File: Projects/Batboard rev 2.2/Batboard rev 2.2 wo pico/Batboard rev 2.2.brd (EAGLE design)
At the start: 101.6 x 68.6 mm, 61 parts, among them J1 1X2-3.5MM, J2 1X2-3.5MM, J3 1X2-3.5MM, J4 1X2-3.5MM, J5 1X2-3.5MM, J6 1X2-3.5MM, U2 TL3472CD, X1 22-23-2081, X17 22-23-2081

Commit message: Updated
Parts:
- moved TPS1 143.0 mm to (31.3, 6.99)
- moved C4 115.4 mm to (30.6, 11.1), turned to 180 degrees
- moved R25 106.0 mm to (2.22, 44.5), turned to 270 degrees
- moved C5 105.1 mm to (25.2, 8.41), turned to 180 degrees
- moved SRR1260-100M1 100.7 mm to (47.1, 7.14), turned to 270 degrees
- moved R5 99.9 mm to (27.3, 2.86)
- moved R3 98.5 mm to (32.4, 2.86)
- moved R6 98.2 mm to (25.2, 5.56), turned to 180 degrees
- moved SHOTTKY1 98.2 mm to (36.5, 11.3)
- moved R7 85.0 mm to (36.4, 7.30), turned to 90 degrees
- moved C9 81.9 mm to (37.5, 2.86)
- moved C6 80.6 mm to (39.2, 7.30), turned to 270 degrees
- moved U$7 74.6 mm to (66.8, 9.21)
- moved R12 73.1 mm to (59.2, 4.60), turned to 90 degrees
- moved C21 72.2 mm to (68.9, 3.49), turned to 270 degrees
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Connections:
- removed net 12V: C2.2, U$5.14
- net +12V: now also C2.2, U$5.14
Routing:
- net +12V: track 104.7 -> 226.7 mm, vias 3 -> 4
- net +5V: track 61.0 -> 103.1 mm, vias 0 -> 1
- net -12V: track 12.1 -> 49.1 mm, vias 1 -> 2
- net N$14: track 19.8 -> 43.5 mm
- net N$16: track 19.3 -> 40.4 mm
- net N$53: track 0.00 -> 20.7 mm
- net N$58: track 0.00 -> 19.7 mm
- net N$18: track 17.6 -> 37.2 mm
- net N$19: track 16.5 -> 34.1 mm
- net N$23: track 15.9 -> 30.9 mm
- net N$27: track 15.4 -> 29.7 mm
- net BATT: track 0.00 -> 13.2 mm
- net N$28: track 15.3 -> 25.8 mm, vias 0 -> 1
- net N$13: track 18.0 -> 26.2 mm
- net N$54: track 0.00 -> 7.82 mm
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
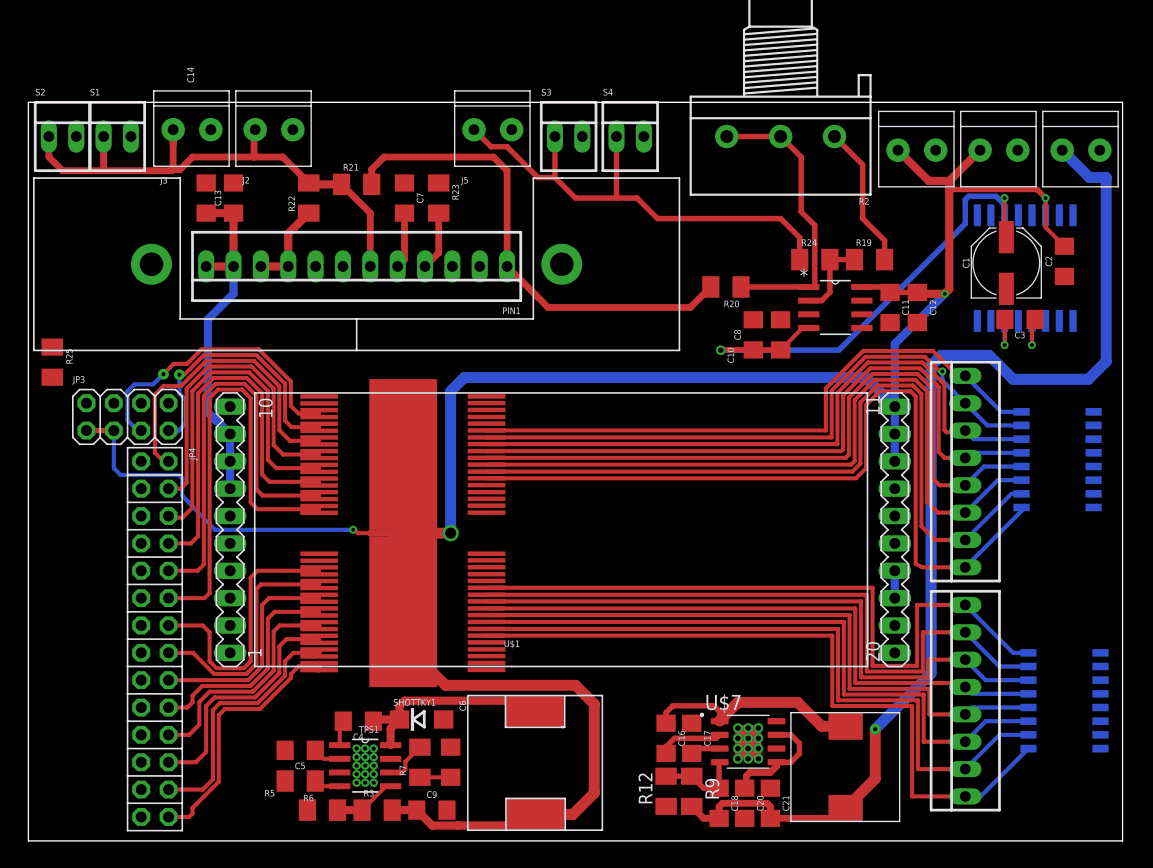
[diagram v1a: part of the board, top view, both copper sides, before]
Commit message: Checked ERC and DRC
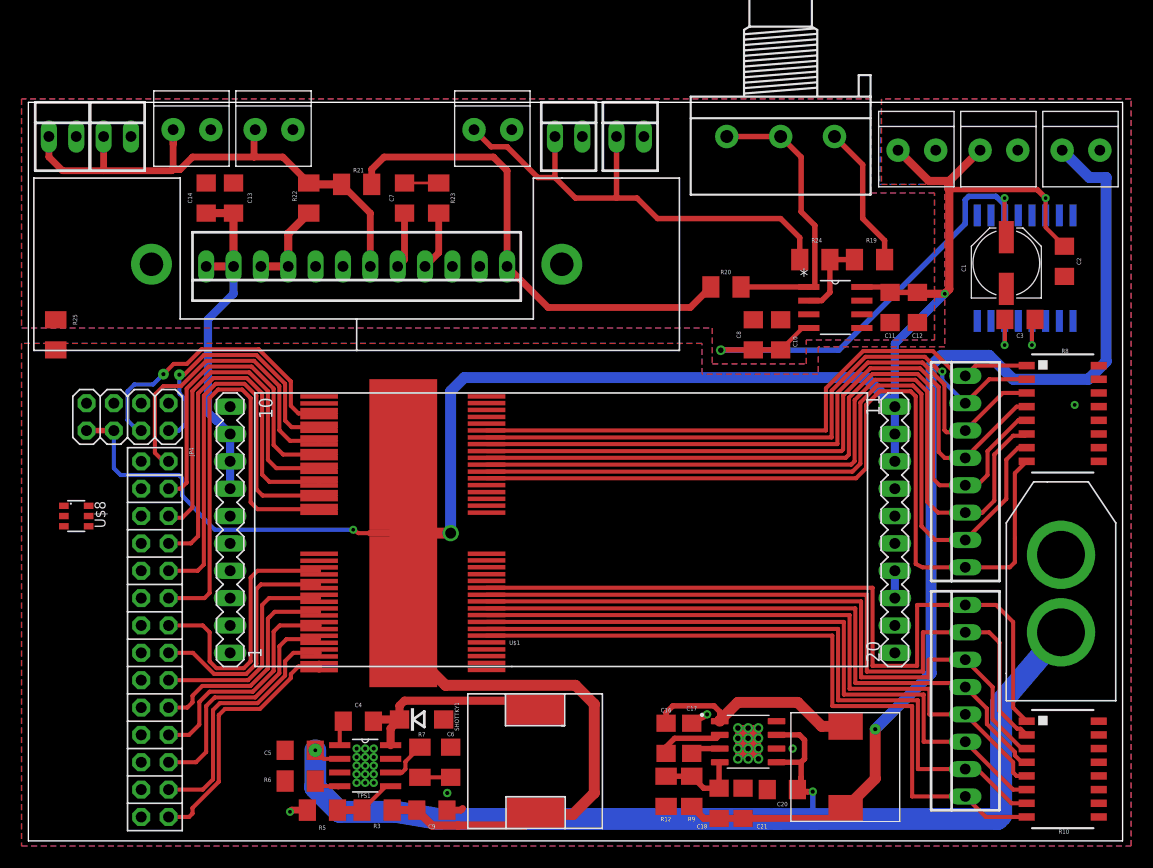
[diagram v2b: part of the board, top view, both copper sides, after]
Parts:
- added U$6: XT60, ultravolt_daughterboard:XT60
- added U$8: DMN2004DMK_DUAL_N-CHANNEL_MOSFET_ARRAY, ultravolt_daughterboard:SOT23-6
- R10, R8: value (none) -> 10K
- moved R10 6.35 mm to (96.0, 6.67), flipped to the top, turned to 270 degrees
- moved R8 4.31 mm to (96.0, 39.7), flipped to the top, turned to 270 degrees
- moved C20 3.72 mm to (70.0, 4.76), turned to 180 degrees
- moved R25 2.56 mm to (2.54, 47.0)
- moved C21 2.54 mm to (66.4, 3.49)
- moved SRR1260-100M1 0.16 mm to (47.1, 7.30)
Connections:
- removed net N$31: U$5.5
- net BATT: now also U$6.POS
- net GND: now also U$5.5, U$6.NEG
- net N$2: now also R10.8; no longer R10.1
- net N$3: now also R10.7; no longer R10.2
- net N$30: now also R8.8; no longer R8.1
- net N$32: now also R10.1; no longer R10.8
- net N$33: now also R10.2; no longer R10.7
- net N$35: now also R10.6; no longer R10.3
- net N$36: now also R10.3; no longer R10.6
- net N$37: now also R10.4; no longer R10.5
- net N$38: now also R10.5; no longer R10.4
- net N$39: now also R8.1; no longer R8.8
- net N$40: now also R8.2; no longer R8.7
- net N$41: now also R8.7; no longer R8.2
- net N$42: now also R8.6; no longer R8.3
- net N$43: now also R8.3; no longer R8.6
- net N$44: now also R8.4; no longer R8.5
- net N$45: now also R8.5; no longer R8.4
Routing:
- net BATT: track 13.2 -> 106.6 mm, vias 0 -> 2
- net N$32: track 65.1 -> 72.2 mm
- net N$30: track 74.8 -> 81.7 mm
- net N$33: track 62.4 -> 68.6 mm
- net GND: track 0.00 -> 4.86 mm, vias 0 -> 5
- net N$42: track 68.6 -> 73.4 mm
- net N$41: track 71.2 -> 75.6 mm
- net N$36: track 60.2 -> 64.5 mm
- net N$37: track 57.9 -> 61.7 mm
- net N$45: track 65.9 -> 69.4 mm
- net N$26: track 0.00 -> 3.18 mm
- net N$38: track 60.4 -> 62.9 mm
- net +5V: track 103.1 -> 100.7 mm
- net N$44: track 63.0 -> 65.2 mm
- net N$35: track 62.2 -> 64.1 mm
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- added copper zone on layer 1, net GND
- added copper zone on layer 16, net GND

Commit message: BOM generation started
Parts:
- added SV1: (no value), con-lstb:MA03-1
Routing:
- net N$9: track 21.4 -> 23.0 mm
- net N$8: track 22.2 -> 23.8 mm
- net N$7: track 23.3 -> 24.9 mm
- net N$6: track 24.5 -> 26.0 mm
- net N$5: track 24.5 -> 26.1 mm
- net N$13: track 26.2 -> 27.7 mm
- net N$12: track 23.0 -> 24.5 mm
- net N$11: track 21.1 -> 22.7 mm
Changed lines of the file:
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@@
 <drawing>
 <settings>
-<setting alwaysvectorfont="yes"/>
+<setting alwaysvectorfont="no"/>
 <setting verticaltext="up"/>
 </settings>
@@
 <attribute name="NAME" x="6.147" y="31.5595" size="1.016" layer="25" ratio="10" rot="R270"/>
 </element>
+<element name="SV1" library="con-lstb" library_urn="urn:adsk.eagle:library:162" package="MA03-1" package3d_urn="urn:adsk.eagle:package:8339/1" value="" x="5.08" y="21.2725" rot="R90">
+<attribute name="MF" value="" x="5.08" y="21.2725" size="1.778" layer="27" rot="R90" display="off"/>
+<attribute name="MPN" value="" x="5.08" y="21.2725" size="1.778" layer="27" rot="R90" display="off"/>
+<attribute name="OC_FARNELL" value="unknown" x="5.08" y="21.2725" size="1.778" layer="27" rot="R90" display="off"/>
+<attribute name="OC_NEWARK" value="unknown" x="5.08" y="21.2725" size="1.778" layer="27" rot="R90" display="off"/>
+</element>
 </elements>
 <signals>
@@
 <wire x1="83.6075" y1="61.2775" x2="85.5125" y2="61.2775" width="0.762" layer="1"/>
 <wire x1="85.5125" y1="61.2775" x2="85.5125" y2="60.48375" width="0.762" layer="1"/>
-<wire x1="85.5125" y1="60.48375" x2="85.5125" y2="51.2225" width="0.762" layer="1"/>
+<wire x1="85.5125" y1="51.2225" x2="85.5125" y2="60.48375" width="0.762" layer="1"/>
 <wire x1="85.5125" y1="51.2225" x2="85.09" y2="50.8" width="0.762" layer="1"/>
 <wire x1="14.2875" y1="32.0675" x2="17.30375" y2="28.8925" width="0.381" layer="16"/>
@@
 <contactref element="U$2" pad="P$36"/>
 <contactref element="U$2" pad="P$35"/>
-<wire x1="26.994" y1="16.493" x2="26.994" y2="16.1925" width="0.508" layer="1"/>
-<wire x1="26.994" y1="16.1925" x2="26.994" y2="15.859" width="0.508" layer="1"/>
 <wire x1="13.024" y1="2.2225" x2="13.0175" y2="2.2225" width="0.508" layer="1"/>
 <wire x1="25.0825" y1="16.1925" x2="26.994" y2="16.1925" width="0.381" layer="1"/>
@@
 <wire x1="13.0175" y1="2.2225" x2="14.9225" y2="2.2225" width="0.381" layer="1"/>
 <wire x1="14.9225" y1="2.2225" x2="15.24" y2="2.54" width="0.381" layer="1"/>
+<wire x1="26.994" y1="16.1925" x2="28.575" y2="16.1925" width="0.381" layer="1"/>
+<wire x1="26.994" y1="16.1925" x2="26.994" y2="16.493" width="0.254" layer="1"/>
+<wire x1="26.994" y1="16.1925" x2="26.994" y2="15.859" width="0.254" layer="1"/>
 </signal>
 <signal name="N$6">
@@
 <wire x1="17.145" y1="5.715" x2="16.1925" y2="4.7625" width="0.381" layer="1"/>
 <wire x1="16.1925" y1="4.7625" x2="13.0175" y2="4.7625" width="0.381" layer="1"/>
+<wire x1="26.994" y1="17.4625" x2="28.575" y2="17.4625" width="0.381" layer="1"/>
 </signal>
 <signal name="N$7">
@@
 <wire x1="16.51" y1="8.255" x2="15.5575" y2="7.3025" width="0.381" layer="1"/>
 <wire x1="15.5575" y1="7.3025" x2="13.0175" y2="7.3025" width="0.381" layer="1"/>
+<wire x1="26.994" y1="18.7325" x2="28.575" y2="18.7325" width="0.381" layer="1"/>
 </signal>
 <signal name="N$8">
@@
 <wire x1="15.875" y1="10.795" x2="14.9225" y2="9.8425" width="0.381" layer="1"/>
 <wire x1="14.9225" y1="9.8425" x2="13.0175" y2="9.8425" width="0.381" layer="1"/>
+<wire x1="26.994" y1="20.0025" x2="28.575" y2="20.0025" width="0.381" layer="1"/>
 </signal>
 <signal name="N$9">
@@
 <wire x1="22.8727" y1="21.2725" x2="22.3901" y2="20.7899" width="0.381" layer="1"/>
 <wire x1="22.3901" y1="20.7899" x2="22.2377" y2="20.6375" width="0.381" layer="1"/>
+<wire x1="26.994" y1="21.2725" x2="28.575" y2="21.2725" width="0.381" layer="1"/>
 </signal>
 <signal name="N$11">
@@
 <wire x1="22.3393" y1="22.5425" x2="21.7043" y2="21.9075" width="0.381" layer="1"/>
 <wire x1="26.994" y1="22.5425" x2="22.3393" y2="22.5425" width="0.381" layer="1"/>
+<wire x1="26.994" y1="22.5425" x2="28.575" y2="22.5425" width="0.381" layer="1"/>
 </signal>
 <signal name="N$12">
@@
 <wire x1="17.24155625" y1="15.50035" x2="15.27940625" y2="17.4625" width="0.381" layer="1"/>
 <wire x1="15.27940625" y1="17.4625" x2="13.0175" y2="17.4625" width="0.381" layer="1"/>
+<wire x1="26.994" y1="23.8125" x2="28.575" y2="23.8125" width="0.381" layer="1"/>
 </signal>
 <signal name="N$13">
@@
 <wire x1="26.994" y1="24.745" x2="26.994" y2="25.0825" width="0.254" layer="1"/>
 <wire x1="26.994" y1="25.0825" x2="26.994" y2="25.395" width="0.254" layer="1"/>
-<wire x1="26.994" y1="25.0825" x2="21.2725" y2="25.0825" width="0.381" layer="1"/>
+<wire x1="26.994" y1="25.0825" x2="26.82875" y2="25.0825" width="0.381" layer="1"/>
+<wire x1="26.82875" y1="25.0825" x2="21.2725" y2="25.0825" width="0.381" layer="1"/>
 <wire x1="21.2725" y1="25.0825" x2="20.6375" y2="24.4475" width="0.381" layer="1"/>
 <wire x1="20.6375" y1="24.4475" x2="20.6375" y2="16.66875" width="0.381" layer="1"/>
@@
 <wire x1="16.8275" y1="19.3675" x2="16.1925" y2="20.0025" width="0.381" layer="1"/>
 <wire x1="16.1925" y1="20.0025" x2="13.0175" y2="20.0025" width="0.381" layer="1"/>
+<wire x1="26.994" y1="25.0825" x2="28.575" y2="25.0825" width="0.381" layer="1"/>
 </signal>
 <signal name="N$14">

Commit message: Updated BOM
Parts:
- moved C9 4.13 mm to (33.3, 2.86)
- moved SHOTTKY1 4.13 mm to (32.4, 11.3)
- moved C4 4.13 mm to (26.5, 11.1)
- moved C5 4.13 mm to (21.1, 8.41)
- moved R5 4.13 mm to (23.2, 2.86)
- moved R6 4.13 mm to (21.1, 5.56)
- moved TPS1 4.13 mm to (27.1, 6.99)
- moved C6 4.13 mm to (35.1, 7.30)
- moved R3 4.13 mm to (28.3, 2.86)
- moved R7 4.13 mm to (32.2, 7.30)
- moved SRR1260-100M1 4.13 mm to (43.0, 7.30)
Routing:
- net BATT: track 106.6 -> 76.2 mm
- net +12V: track 226.8 -> 215.2 mm

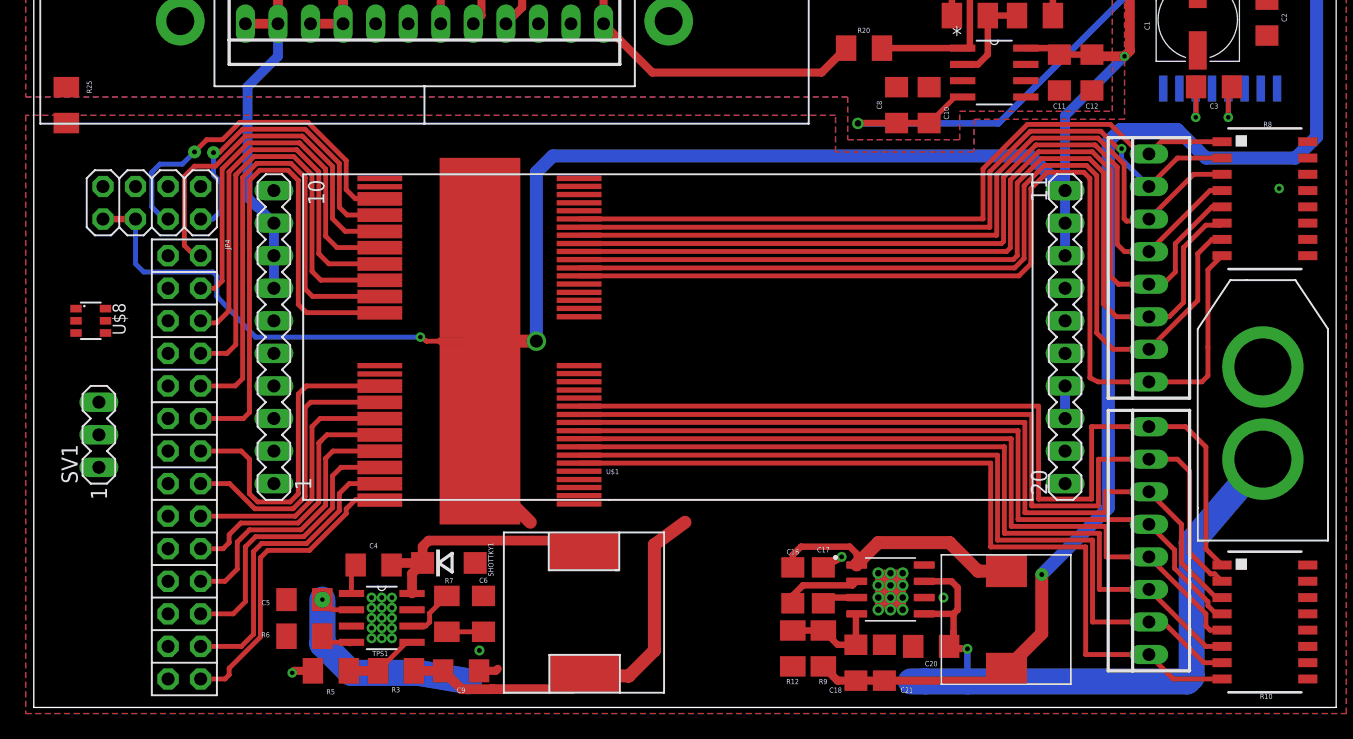
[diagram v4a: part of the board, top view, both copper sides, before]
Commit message: Updated capacitors for switching step down regulators
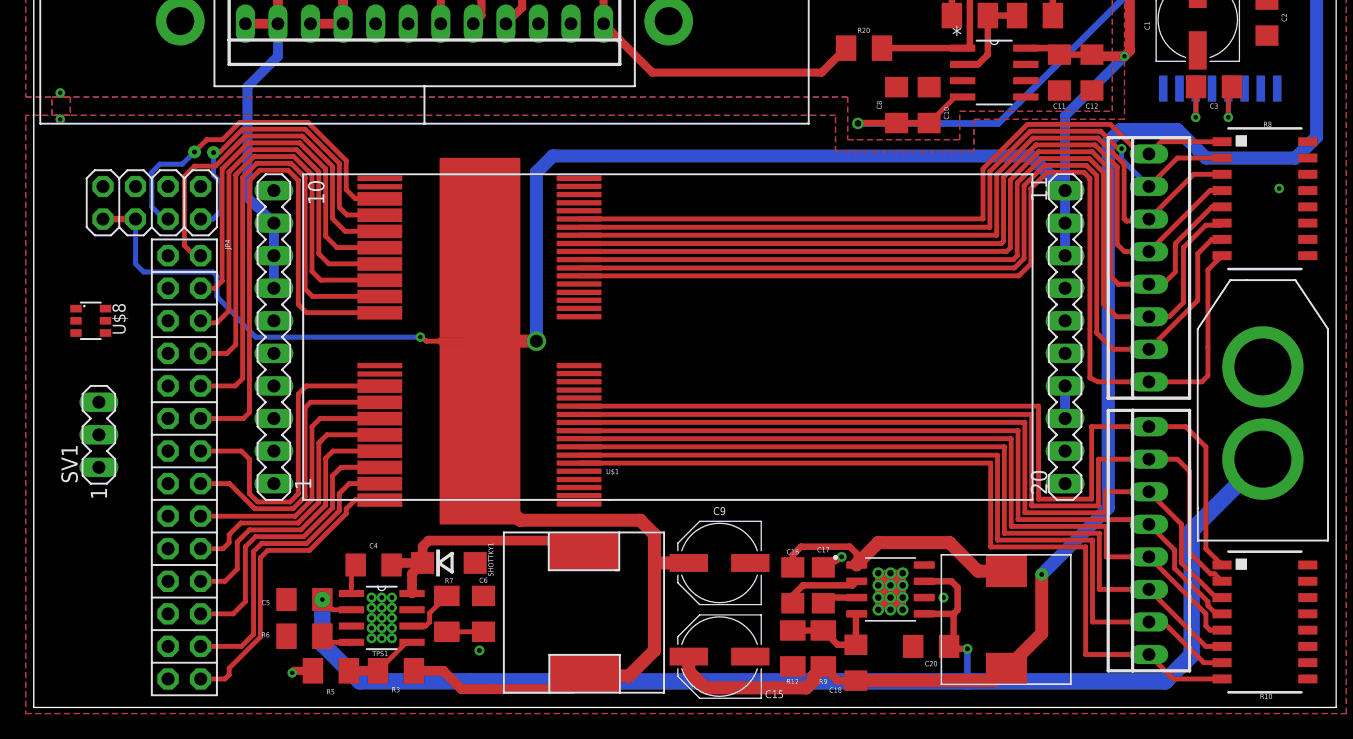
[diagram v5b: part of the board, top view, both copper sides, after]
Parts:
- removed C21: 100uF, SparkFun-Capacitors:1206
- removed R25: 0, adafruit:M1206
- added C15: 100uF, SparkFun-Capacitors:PANASONIC_D
- C9: value 13.9uF -> 100uF; device SparkFun-Capacitors:1206 -> SparkFun-Capacitors:PANASONIC_D
- moved C9 21.8 mm to (53.5, 11.3), turned to 180 degrees
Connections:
- net +12V: now also C9.+; no longer C9.1
- net +5V: now also C15.+; no longer C21.2
- net GND: now also C15.-, C9.-; no longer C21.1, C9.2, R25.1, R25.2
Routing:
- net BATT: track 76.2 -> 108.2 mm
- net +5V: track 100.7 -> 113.8 mm
- net +12V: track 215.2 -> 226.4 mm
- net GND: track 4.86 -> 3.34 mm, vias 5 -> 7
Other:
- board text added: "+"
- board text added: "-"

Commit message: Updated LEDS
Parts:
- removed SV1: (no value), con-lstb:MA03-1
- added LED1, LED2, LED3: (no value), eagle-ltspice:LED_1206
- added R1, R11, R4: 500, resistor:R1206
- added R13, R14, R15: 1K, resistor:R1206
- added U$9: DMN2004DMK_DUAL_N-CHANNEL_MOSFET_ARRAY, ultravolt_daughterboard:SOT23-6
- R2: value (none) -> 50K
- moved U$8 11.7 mm to (3.17, 18.6)
- moved PIN1 1.59 mm to (30.5, 51.8)
- moved S1 0.32 mm to (8.57, 65.4)
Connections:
- new net 5V: R1.2, R11.2, R4.2
- new net N$31: LED1.A, R1.1
- new net N$84: LED2.A, R4.1
- new net N$85: LED3.A, R11.1
- new net N$86: LED3.C, U$9.6
- new net N$87: LED1.C, U$8.6
- new net N$88: LED2.C, U$8.3
- net +12V: now also R13.2, U$8.5
- net +5V: now also R14.2, U$8.2
- net -12V: now also R15.1, U$9.4
- net GND: now also R13.1, R14.1, R15.2, U$8.1, U$8.4, U$9.5
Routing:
- net -12V: track 49.1 -> 133.9 mm, vias 2 -> 3
- net +5V: track 113.8 -> 173.6 mm, vias 1 -> 3
- net +12V: track 226.4 -> 252.3 mm, vias 4 -> 5
- net N$15: track 27.1 -> 45.4 mm, vias 0 -> 2
- net N$87: track 0.00 -> 12.7 mm
- net N$88: track 0.00 -> 10.1 mm
- net N$85: track 0.00 -> 10.0 mm
- net N$86: track 0.00 -> 7.91 mm
- net N$84: track 0.00 -> 6.67 mm
- net BATT: track 108.2 -> 113.3 mm
- net 5V: track 0.00 -> 4.76 mm
- net N$31: track 0.00 -> 3.10 mm
- net GND: track 3.34 -> 4.95 mm, vias 7 -> 9
- net N$22: track 50.9 -> 52.5 mm
- net N$20: track 8.28 -> 9.87 mm
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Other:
- board size 101.6 x 68.6 mm -> 101.6 x 68.9 mm
- board text added: "-12V"
- board text added: "12V"
- board text added: "5V"
- board text added: "Input"
- board text added: "Output"
- board text added: "PRE AMP"

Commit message: Update with Microphones
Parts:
- removed J4: 1X2-3.5MM, adafruit:1X2-3.5MM
- removed S1: 22-23-2021, con-molex:22-23-2021
- removed SLF1: 10uH, Inductors:10.1*10.1
- added SRR1260-100M2: 10uH, Inductors:12.5*12.5
- moved R12 13.5 mm to (58.4, 18.1), turned to 270 degrees
- moved C20 11.1 mm to (58.9, 5.08), turned to 270 degrees
- moved C16 8.99 mm to (64.5, 16.8), turned to 180 degrees
- moved C17 8.61 mm to (60.8, 18.1)
- moved J1 6.25 mm to (84.5, 66.7)
- moved U$7 6.18 mm to (61.3, 11.9), turned to 270 degrees
- moved S2 6.17 mm to (9.05, 67.3)
- moved J6 5.40 mm to (93.0, 66.7)
- moved J2 5.05 mm to (27.8, 67.2)
- moved J3 3.36 mm to (18.4, 67.2)
- moved R10 3.33 mm to (96.0, 10.0)
- moved C18 3.27 mm to (61.3, 5.08)
- moved U$6 3.02 mm to (95.9, 26.2)
- moved C2 2.78 mm to (97.6, 56.2)
- moved R8 2.70 mm to (95.9, 42.4)
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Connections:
- net +12V: no longer J4.1
- net +5V: now also SRR1260-100M2.P$2; no longer SLF1.P$2
- net -12V: now also C1.-; no longer C1.+
- net GND: now also C1.+, TPS1.7; no longer C1.-, J4.2, S1.2
- net N$22: no longer S1.1
- net N$53: now also SRR1260-100M2.P$1; no longer SLF1.P$1
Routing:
- net N$54: track 7.82 -> 22.8 mm, vias 0 -> 2
- net +5V: track 173.6 -> 187.1 mm, vias 3 -> 4
- net N$53: track 20.7 -> 14.7 mm
- net +12V: track 252.3 -> 248.3 mm
- net N$52: track 6.05 -> 2.76 mm
- net N$58: track 19.6 -> 22.6 mm
- net BATT: track 113.3 -> 115.9 mm
- net N$17: track 45.8 -> 43.4 mm
- net N$38: track 62.9 -> 61.1 mm
- net N$20: track 9.87 -> 8.32 mm
- net N$35: track 64.1 -> 62.5 mm
- net N$22: track 52.5 -> 51.1 mm
- net N$32: track 72.2 -> 70.8 mm
- net N$4: track 46.0 -> 44.8 mm
- net V+: track 32.5 -> 31.4 mm
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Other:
- board size 101.6 x 68.9 mm -> 101.6 x 71.1 mm
- board text added: "Bat-Board Rev 2.2 July 2018"
- board text added: "C11"
- board text added: "Lucas Mun"

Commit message: Havent done this in a while
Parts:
- TPS1: value TPS54560(8) -> TPS54560
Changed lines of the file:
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@@
 <?xml version="1.0" encoding="utf-8"?>
 <!DOCTYPE eagle SYSTEM "eagle.dtd">
-<eagle version="9.1.1">
+<eagle version="9.1.3">
 <drawing>
 <settings>
@@
 </element>
 <element name="J5" library="adafruit" package="1X2-3.5MM" value="1X2-3.5MM" x="42.06875" y="66.9925" smashed="yes" rot="R180"/>
-<element name="TPS1" library="SOIC127P600X175-8N" package="SOIC127P600X175-8N" value="TPS54560(8)" x="27.14625" y="8.89" smashed="yes">
+<element name="TPS1" library="SOIC127P600X175-8N" package="SOIC127P600X175-8N" value="TPS54560" x="27.14625" y="8.89" smashed="yes">
 <attribute name="NAME" x="26.244" y="11.625490625" size="0.6096" layer="25" font="vector" ratio="10" rot="SR0"/>
 </element>
@@
 <via x="4.28625" y="6.82625" extent="1-16" drill="0.508"/>
 <contactref element="TPS1" pad="7"/>
-<wire x1="35.08375" y1="10.6075" x2="29.50845" y2="9.525" width="0" layer="19" extent="1-1"/>
 </signal>
 <signal name="+12V">
